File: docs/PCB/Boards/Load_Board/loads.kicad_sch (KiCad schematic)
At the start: 117 parts, among them J17 Conn_01x01_Pin, J18 Conn_01x01_Pin, J19 Conn_01x01_Pin, J20 Conn_01x01_Pin, J21 Conn_01x01_Pin, J22 Conn_01x01_Pin, J23 Conn_01x01_Pin, J24 Conn_01x01_Pin, J25 Conn_01x01_Pin, J26 Conn_01x01_Pin, J27 Conn_01x01_Pin, J28 Conn_01x01_Pin, J29 Conn_01x01_Pin, J30 Conn_01x01_Pin, J31 Conn_01x01_Pin, J32 Conn_01x01_Pin, J33 Conn_01x01_Pin, J34 Conn_01x01_Pin, J35 Conn_01x01_Pin, J36 Conn_01x01_Pin, J37 Conn_01x01_Pin, J38 Conn_01x01_Pin, J39 Conn_01x01_Pin, J40 Conn_01x01_Pin, J41 Conn_01x01_Pin, J42 Conn_01x01_Pin, J43 Conn_01x01_Pin, J44 Conn_01x01_Pin, J45 Conn_01x01_Pin, J46 Conn_01x01_Pin, J47 Conn_01x01_Pin, J48 Conn_01x01_Pin, J49 Conn_01x01_Pin, J50 Conn_01x01_Pin, J51 Conn_01x01_Pin, J52 Conn_01x01_Pin, J53 Conn_01x01_Pin, J54 Conn_01x01_Pin, J55 Conn_01x01_Pin, J56 Conn_01x01_Pin, J57 Conn_01x01_Pin, J58 Conn_01x01_Pin, J59 Conn_01x01_Pin, J60 Conn_01x01_Pin, J61 Conn_01x01_Pin, J62 Conn_01x01_Pin, J63 Conn_01x01_Pin, J64 Conn_01x01_Pin, J65 Conn_01x01_Pin, J66 Conn_01x01_Pin, J67 Conn_01x01_Pin, J68 Conn_01x01_Pin, J69 Conn_01x01_Pin, J70 Conn_01x01_Pin, J71 Conn_01x01_Pin, J72 Conn_01x01_Pin, J73 Conn_01x01_Pin, J74 Conn_01x01_Pin, J75 Conn_01x01_Pin, J76 Conn_01x01_Pin, J77 Conn_01x01_Pin, J78 Conn_01x01_Pin, J79 Conn_01x01_Pin, J80 Conn_01x01_Pin, J81 Conn_01x01_Pin, J82 Conn_01x01_Pin, J83 Conn_01x01_Pin, J84 Conn_01x01_Pin, J85 Conn_01x01_Pin, J86 Conn_01x01_Pin, J87 Conn_01x01_Pin, J88 Conn_01x01_Pin, Q7 BSS138, Q8 BSS138, SW1 Tact Switch 6x6mm / 13mm, Y1 Crystal, Y2 Crystal, Y3 Crystal

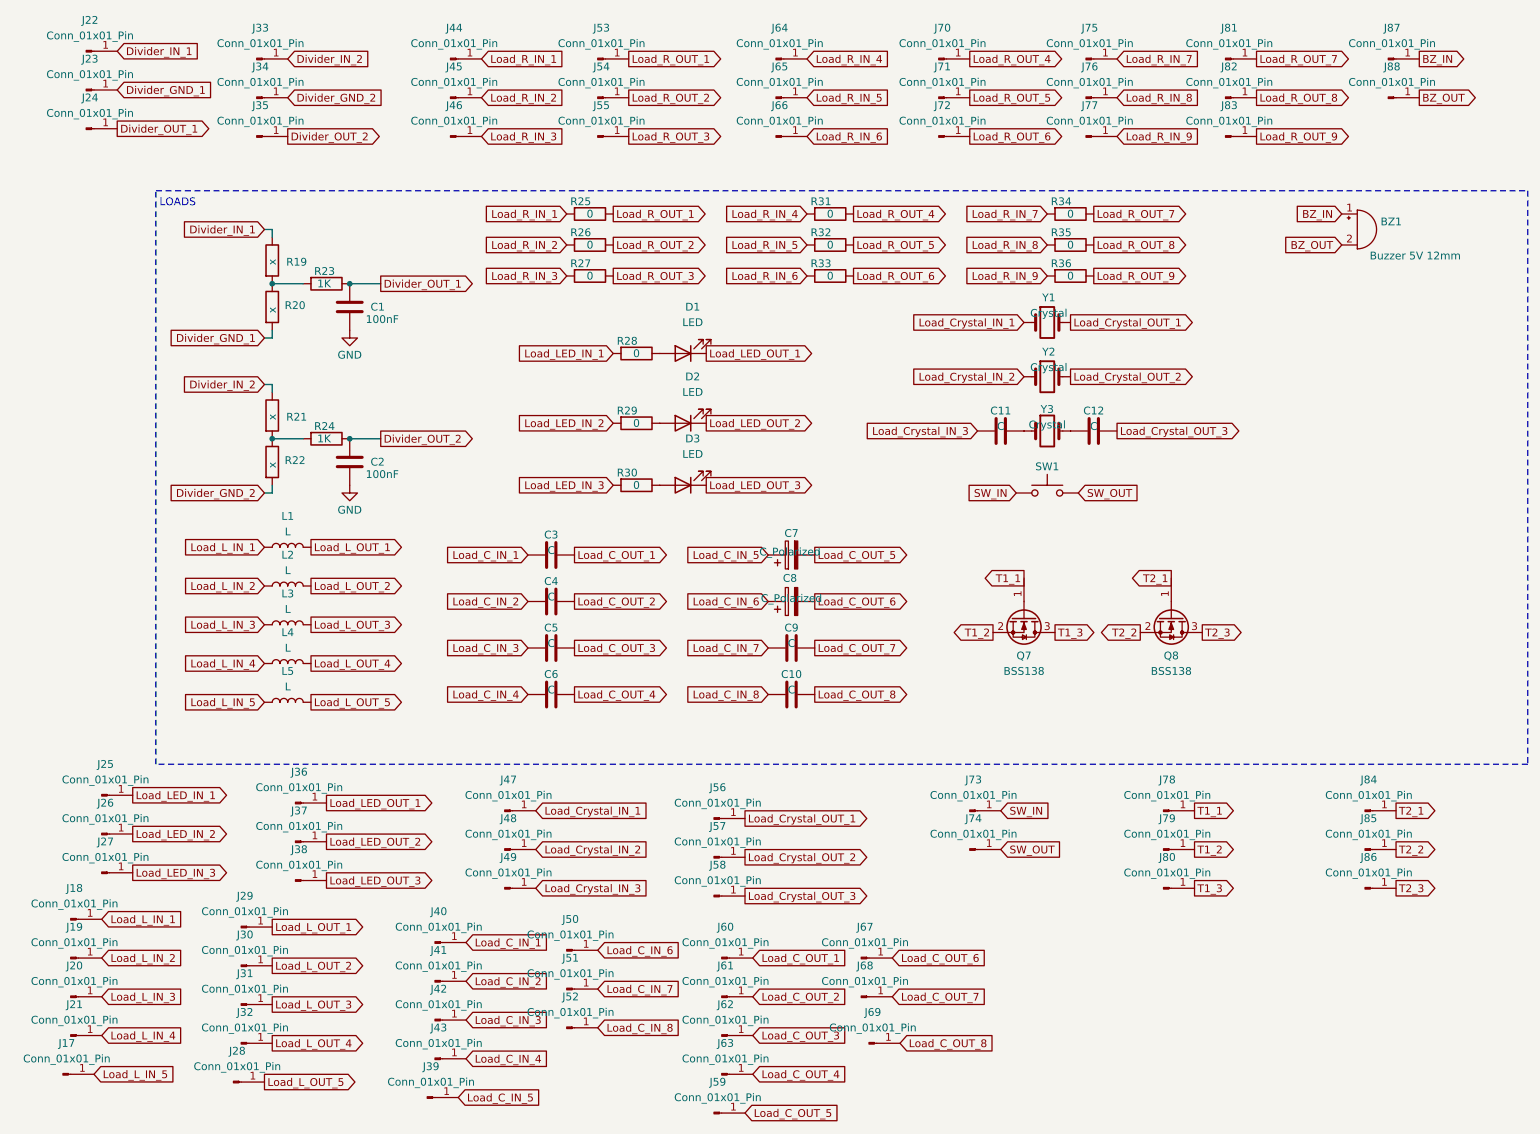
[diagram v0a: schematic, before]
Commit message: Load board and ATMega Board added
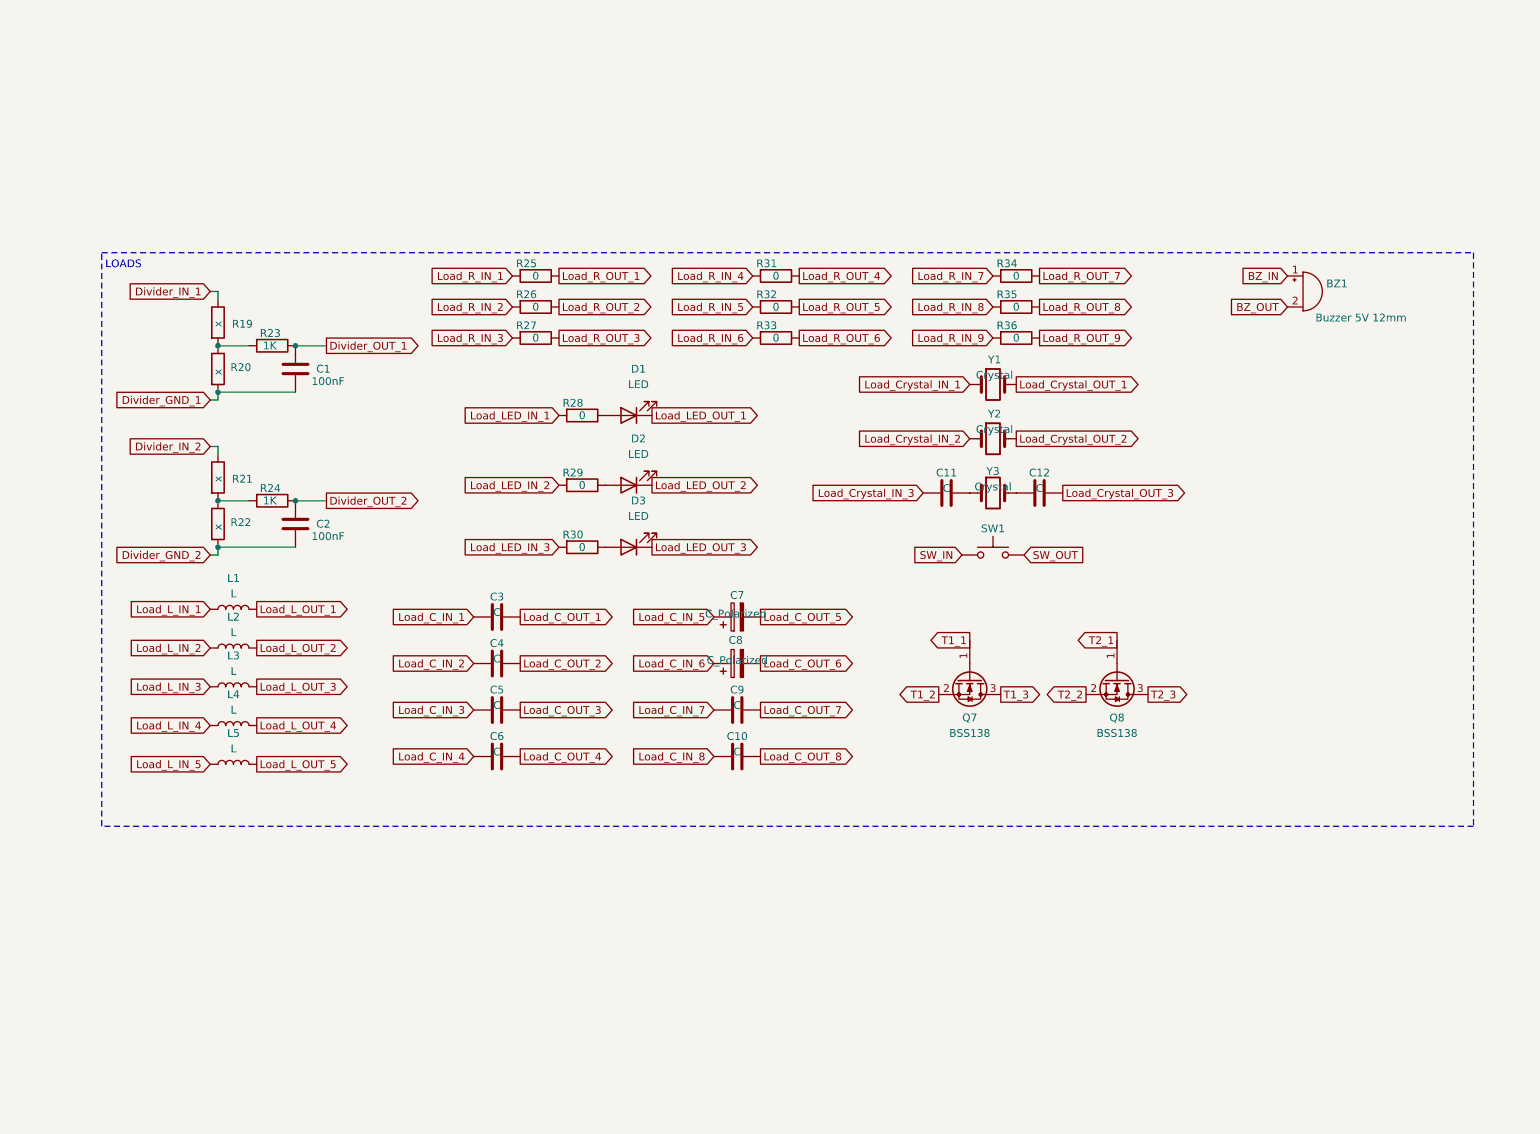
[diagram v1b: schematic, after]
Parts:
- removed J17, J18, J19, J20, J21, J22, J23, J24, J25, J26, J27, J28, J29, J30, J31, J32, J33, J34, J35, J36, J37, J38, J39, J40, J41, J42, J43, J44, J45, J46, J47, J48, J49, J50, J51, J52, J53, J54, J55, J56, J57, J58, J59, J60, J61, J62, J63, J64, J65, J66, J67, J68, J69, J70, J71, J72, J73, J74, J75, J76, J77, J78, J79, J80, J81, J82, J83, J84, J85, J86, J87, J88: Conn_01x01_Pin, Connector_PinHeader_2.54mm:PinHeader_1x01_P2.54mm_Vertical, symbol Connector:Conn_01x01_Pin
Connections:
- net Divider_GND_1: now also C1.2
- net Divider_GND_2: now also C2.2
- removed net GND: C1.2, C2.2
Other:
- company: (none) -> PKl
- title: (none) -> Loads
- moved on the sheet: BZ1, C1, C10, C11, C12, C2, C3, C4, C5, C6, C7, C8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

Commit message: Hardware docs updated.
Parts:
- added RV1, RV2, RV3: R_Potentiometer, Potentiometer_THT:Potentiometer_Runtron_RM-065_Vertical, symbol Device:R_Potentiometer
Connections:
- new net RV1_1: RV1.1
- new net RV1_2: RV1.2
- new net RV1_3: RV1.3
- new net RV2_1: RV2.1
- new net RV2_2: RV2.2
- new net RV2_3: RV2.3
- new net RV3_1: RV3.1
- new net RV3_2: RV3.2
- new net RV3_3: RV3.3
